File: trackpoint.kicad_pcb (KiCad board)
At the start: 2 copper layers, 27.5 x 24 mm, 9 parts

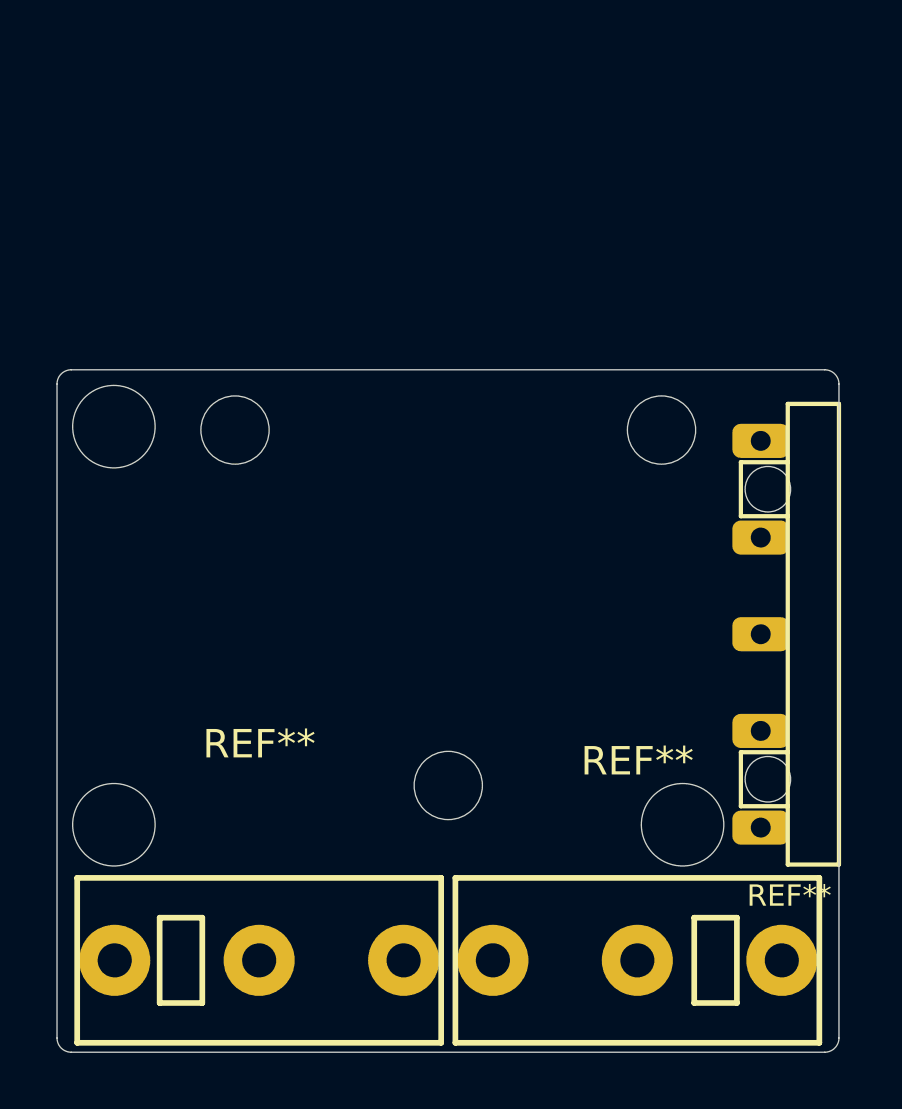
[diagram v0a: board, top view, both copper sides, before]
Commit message: Update board based on new CAD design.
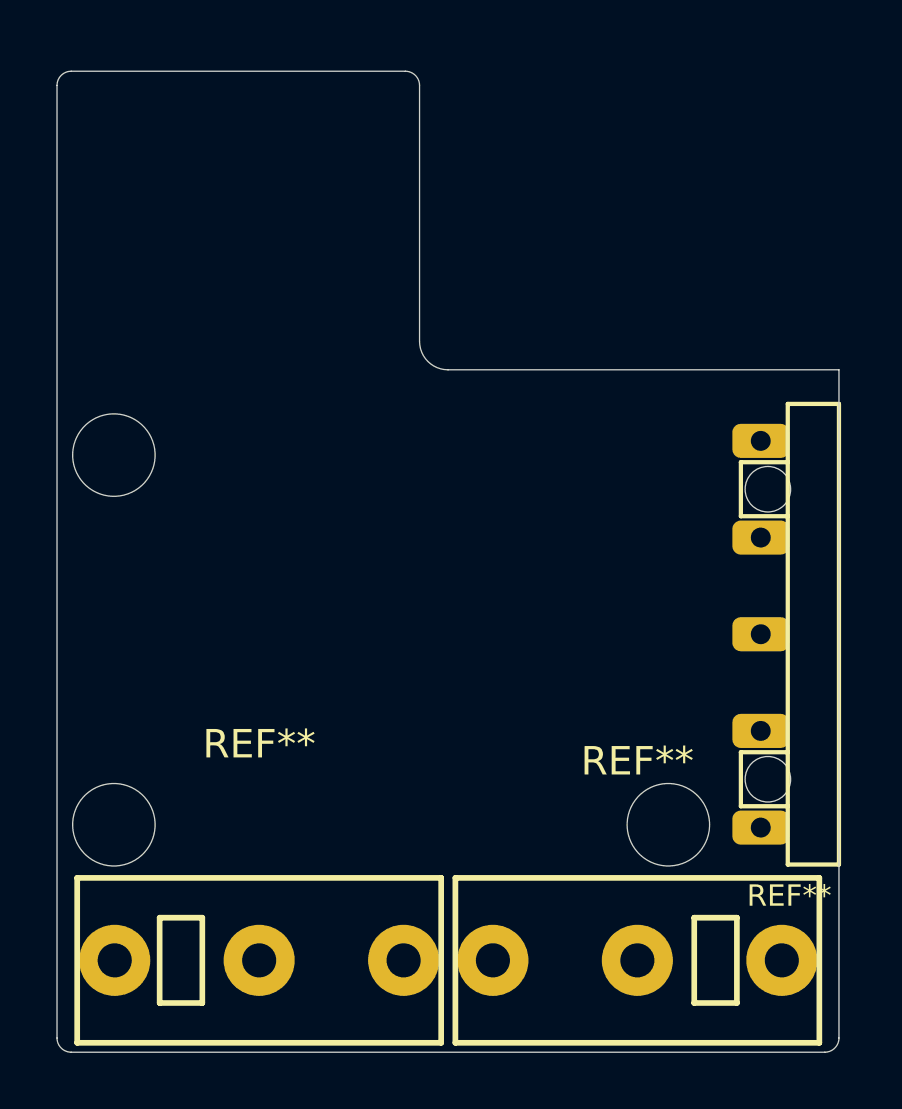
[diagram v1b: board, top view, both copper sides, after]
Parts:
- removed the ? at (194.2, 125.5)
- removed the ? at (206.0, 138.1)
- removed the ? at (213.5, 125.6)
- removed the ? at (198.5, 125.6)
- removed the ? at (214.2, 139.5)
- added ?: , UGL:hole_2.9000000953674316mm, F.Cu at (194.2, 126.5)
- added ?: , UGL:hole_2.9000000953674316mm, F.Cu at (213.8, 139.5)
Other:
- board size 27.5 x 24 mm -> 27.5 x 34.5 mm
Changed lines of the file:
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@@
   (general
     (thickness 1.6)
-    (drawings 9)
+    (drawings 20)
     (tracks 0)
     (zones 0)
-    (modules 9)
+    (modules 6)
     (nets 1)
   )
@@
   )
   (module UGL:hole_2.9000000953674316mm locked (layer F.Cu)
-    (at 194.25 125.5)
+    (at 194.25 126.5)
     (attr virtual)
     (fp_text reference "" (at 0 0) (layer F.SilkS)
@@
       (clearance 0.00001))
   )
-  (module UGL:hole_2.4000000953674316mm locked (layer F.Cu)
-    (at 206.010002 138.119003)
-    (attr virtual)
-    (fp_text reference "" (at 0 0) (layer F.SilkS)
-      (effects (font (size 1.27 1.27) (thickness 0.15)))
-    )
-    (fp_text value "" (at 0 0) (layer F.SilkS)
-      (effects (font (size 1.27 1.27) (thickness 0.15)))
-    )
-    (pad "" np_thru_hole circle (at 0 0) (size 2.4 2.4) (drill 2.4) (layers *.Cu *.Mask F.SilkS)
-      (clearance 0.00001))
-  )
-  (module UGL:hole_2.4000000953674316mm locked (layer F.Cu)
-    (at 213.510002 125.619003)
-    (attr virtual)
-    (fp_text reference "" (at 0 0) (layer F.SilkS)
-      (effects (font (size 1.27 1.27) (thickness 0.15)))
-    )
-    (fp_text value "" (at 0 0) (layer F.SilkS)
-      (effects (font (size 1.27 1.27) (thickness 0.15)))
-    )
-    (pad "" np_thru_hole circle (at 0 0) (size 2.4 2.4) (drill 2.4) (layers *.Cu *.Mask F.SilkS)
-      (clearance 0.00001))
-  )
-  (module UGL:hole_2.4000000953674316mm locked (layer F.Cu)
-    (at 198.510002 125.619003)
-    (attr virtual)
-    (fp_text reference "" (at 0 0) (layer F.SilkS)
-      (effects (font (size 1.27 1.27) (thickness 0.15)))
-    )
-    (fp_text value "" (at 0 0) (layer F.SilkS)
-      (effects (font (size 1.27 1.27) (thickness 0.15)))
-    )
-    (pad "" np_thru_hole circle (at 0 0) (size 2.4 2.4) (drill 2.4) (layers *.Cu *.Mask F.SilkS)
-      (clearance 0.00001))
-  )
   (module UGL:hole_2.9000000953674316mm locked (layer F.Cu)
-    (at 214.25 139.5)
+    (at 213.75 139.5)
     (attr virtual)
     (fp_text reference "" (at 0 0) (layer F.SilkS)
@@
       (clearance 0.00001))
   )
+  (gr_line (start 204.5 113) (end 192.75 113) (angle 90) (layer Edge.Cuts) (width 0.01))
+  (gr_line (start 192.25 113.5) (end 192.25 147) (angle 90) (layer Edge.Cuts) (width 0.01))
+  (gr_line (start 219.75 123.5) (end 206 123.5) (angle 90) (layer Edge.Cuts) (width 0.01))
   (gr_text "PCB ID: trackpoint_main_0.1.0" (at 206.1 146.5) (layer B.SilkS)
     (effects (font (size 1 1) (thickness 0.2)) (justify mirror))
   )
-  (gr_arc (start 192.75 124.000007) (end 192.75 123.5) (angle -90.00451968) (layer Edge.Cuts) (width 0.01))
   (gr_arc (start 192.75 146.999993) (end 192.25 147) (angle -89.99010657) (layer Edge.Cuts) (width 0.01))
   (gr_arc (start 219.25 146.999993) (end 219.25 147.5) (angle -90.00451968) (layer Edge.Cuts) (width 0.01))
-  (gr_arc (start 219.25 124.000007) (end 219.75 124) (angle -89.99010657) (layer Edge.Cuts) (width 0.01))
-  (gr_line (start 219.25 123.5) (end 192.75 123.5) (angle 90) (layer Edge.Cuts) (width 0.01))
-  (gr_line (start 192.25 124) (end 192.25 147) (angle 90) (layer Edge.Cuts) (width 0.01))
   (gr_line (start 192.75 147.5) (end 219.25 147.5) (angle 90) (layer Edge.Cuts) (width 0.01))
-  (gr_line (start 219.75 147) (end 219.75 124) (angle 90) (layer Edge.Cuts) (width 0.01))
+  (gr_circle (center 210.760002 135.119003) (end 210.760002 137.019003) (layer F.Adhes) (width 0.01))
+  (gr_circle (center 201.260002 135.119003) (end 201.260002 137.019003) (layer F.Adhes) (width 0.01))
+  (gr_circle (center 194.25 139.5) (end 195.9 139.5) (layer Eco1.User) (width 0.01))
+  (gr_circle (center 213.75 139.5) (end 215.4 139.5) (layer Eco1.User) (width 0.01))
+  (gr_circle (center 194.25 126.5) (end 195.9 126.5) (layer Eco1.User) (width 0.01))
+  (gr_circle (center 201.260002 125.619003) (end 201.260002 127.519003) (layer F.Adhes) (width 0.01))
+  (gr_circle (center 210.760002 125.619003) (end 210.760002 127.519003) (layer F.Adhes) (width 0.01))
+  (gr_circle (center 194.199997 118.468994) (end 194.199997 118.718994) (layer F.Adhes) (width 0.01))
+  (gr_arc (start 205.999992 122.500001) (end 205 122.5) (angle -90) (layer Edge.Cuts) (width 0.01))
+  (gr_line (start 205 122.5) (end 205 113.5) (angle 90) (layer Edge.Cuts) (width 0.01))
+  (gr_arc (start 204.5 113.500007) (end 205 113.5) (angle -90) (layer Edge.Cuts) (width 0.01))
+  (gr_arc (start 192.75 113.500007) (end 192.75 113) (angle -90) (layer Edge.Cuts) (width 0.01))
+  (gr_line (start 219.75 147) (end 219.75 123.5) (angle 90) (layer Edge.Cuts) (width 0.01))
 )

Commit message: Add FFC connector.
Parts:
- added REF**: 84981-8, ugl:84981-8, F.Cu at (194.2, 118.5)
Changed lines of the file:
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@@
   (general
     (thickness 1.6)
-    (drawings 20)
+    (drawings 19)
     (tracks 0)
     (zones 0)
-    (modules 6)
+    (modules 7)
     (nets 1)
   )
   (page A3)
   (title_block
-    (title "UHK Trackpoint Module - Main")
+    (title "UHK Trackpoint Module")
     (rev 0.1.0)
     (company "Ultimate Gadget Laboratories Kft.")
@@
     (uvia_drill 0.127)
   )
+  (module ugl:84981-8 (layer F.Cu)
+    (at 194.199997 118.468994 270)
+    (descr "FFC connector")
+    (fp_text reference REF** (at 0 -7.800003 90) (layer F.SilkS)
+      (effects (font (size 0.75 0.75) (thickness 0.15)))
+    )
+    (fp_text value 84981-8 (at 0 0.8 90) (layer F.SilkS)
+      (effects (font (size 0.75 0.75) (thickness 0.15)))
+    )
+    (fp_line (start 5.5 -5.6) (end 4 -5.6) (layer F.SilkS) (width 0.15))
+    (fp_line (start -5.5 -5.6) (end -4 -5.6) (layer F.SilkS) (width 0.15))
+    (fp_line (start -4.5 0) (end 4.5 0) (layer F.SilkS) (width 0.15))
+    (fp_line (start 5.5 -1.8) (end 5.5 -5.6) (layer F.SilkS) (width 0.15))
+    (fp_line (start -5.5 -1.8) (end -5.5 -5.6) (layer F.SilkS) (width 0.15))
+    (pad 5 smd rect (at 0.5 -5.95 270) (size 0.6 1.7) (layers F.Cu F.Paste F.Mask))
+    (pad 4 smd rect (at -0.5 -5.95 270) (size 0.6 1.7) (layers F.Cu F.Paste F.Mask))
+    (pad 6 smd rect (at 1.5 -5.95 270) (size 0.6 1.7) (layers F.Cu F.Paste F.Mask))
+    (pad 3 smd rect (at -1.5 -5.95 270) (size 0.6 1.7) (layers F.Cu F.Paste F.Mask))
+    (pad "" smd rect (at 5.3 -0.7 270) (size 1.2 1.8) (layers F.Cu F.Paste F.Mask))
+    (pad "" smd rect (at -5.3 -0.7 270) (size 1.2 1.8) (layers F.Cu F.Paste F.Mask))
+    (pad 1 smd rect (at -3.5 -5.95 270) (size 0.6 1.7) (layers F.Cu F.Paste F.Mask))
+    (pad 8 smd rect (at 3.5 -5.95 270) (size 0.6 1.7) (layers F.Cu F.Paste F.Mask))
+    (pad 7 smd rect (at 2.5 -5.95 270) (size 0.6 1.7) (layers F.Cu F.Paste F.Mask))
+    (pad 2 smd rect (at -2.5 -5.95 270) (size 0.6 1.7) (layers F.Cu F.Paste F.Mask))
+  )
   (module ugl:CMI126603D08 locked (layer F.Cu)
     (at 199.360001 144.268997)
@@
   (gr_line (start 219.75 123.5) (end 206 123.5) (angle 90) (layer Edge.Cuts) (width 0.01))
   (gr_text "PCB ID: trackpoint_main_0.1.0" (at 206.1 146.5) (layer B.SilkS)
-    (effects (font (size 1 1) (thickness 0.2)) (justify mirror))
+    (effects (font (size 0.75 0.75) (thickness 0.15)) (justify mirror))
   )
   (gr_arc (start 192.75 146.999993) (end 192.25 147) (angle -89.99010657) (layer Edge.Cuts) (width 0.01))
@@
   (gr_circle (center 201.260002 125.619003) (end 201.260002 127.519003) (layer F.Adhes) (width 0.01))
   (gr_circle (center 210.760002 125.619003) (end 210.760002 127.519003) (layer F.Adhes) (width 0.01))
-  (gr_circle (center 194.199997 118.468994) (end 194.199997 118.718994) (layer F.Adhes) (width 0.01))
   (gr_arc (start 205.999992 122.500001) (end 205 122.5) (angle -90) (layer Edge.Cuts) (width 0.01))
   (gr_line (start 205 122.5) (end 205 113.5) (angle 90) (layer Edge.Cuts) (width 0.01))

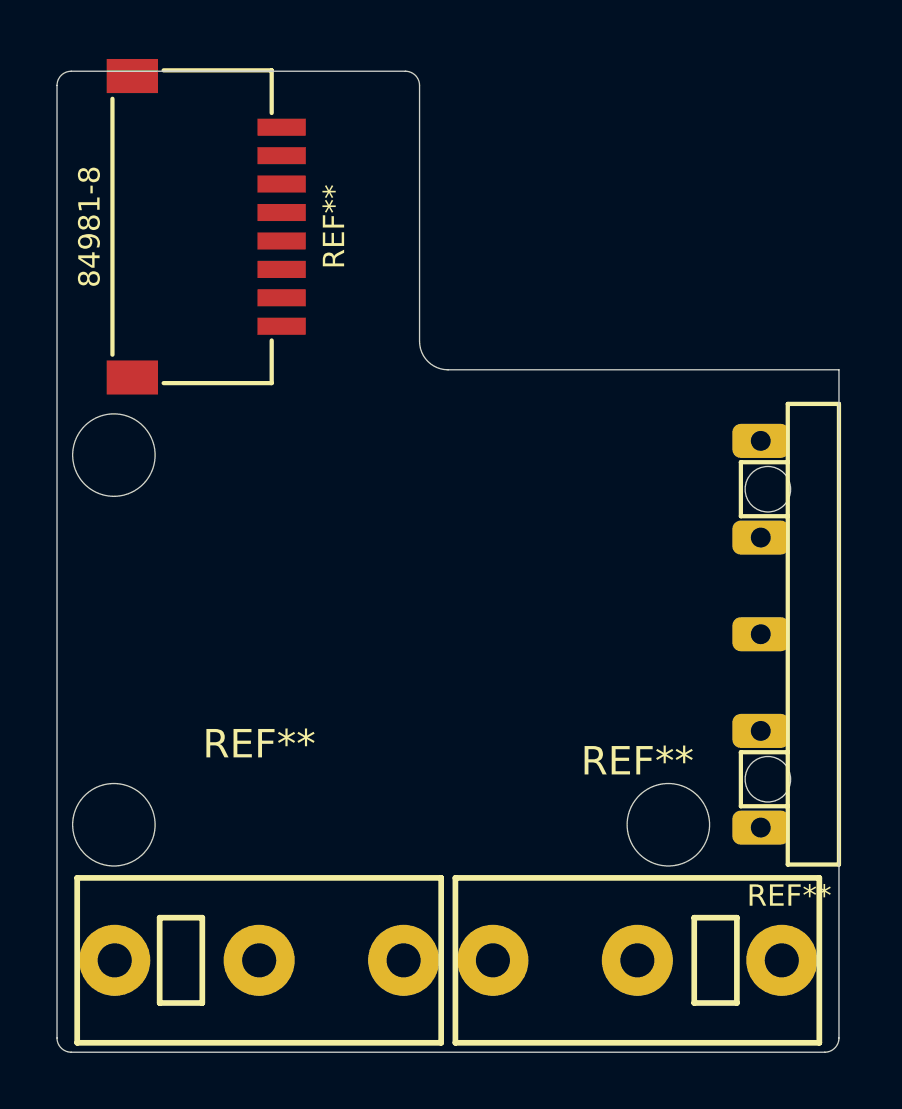
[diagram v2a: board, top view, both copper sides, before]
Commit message: Convert circles to holes.
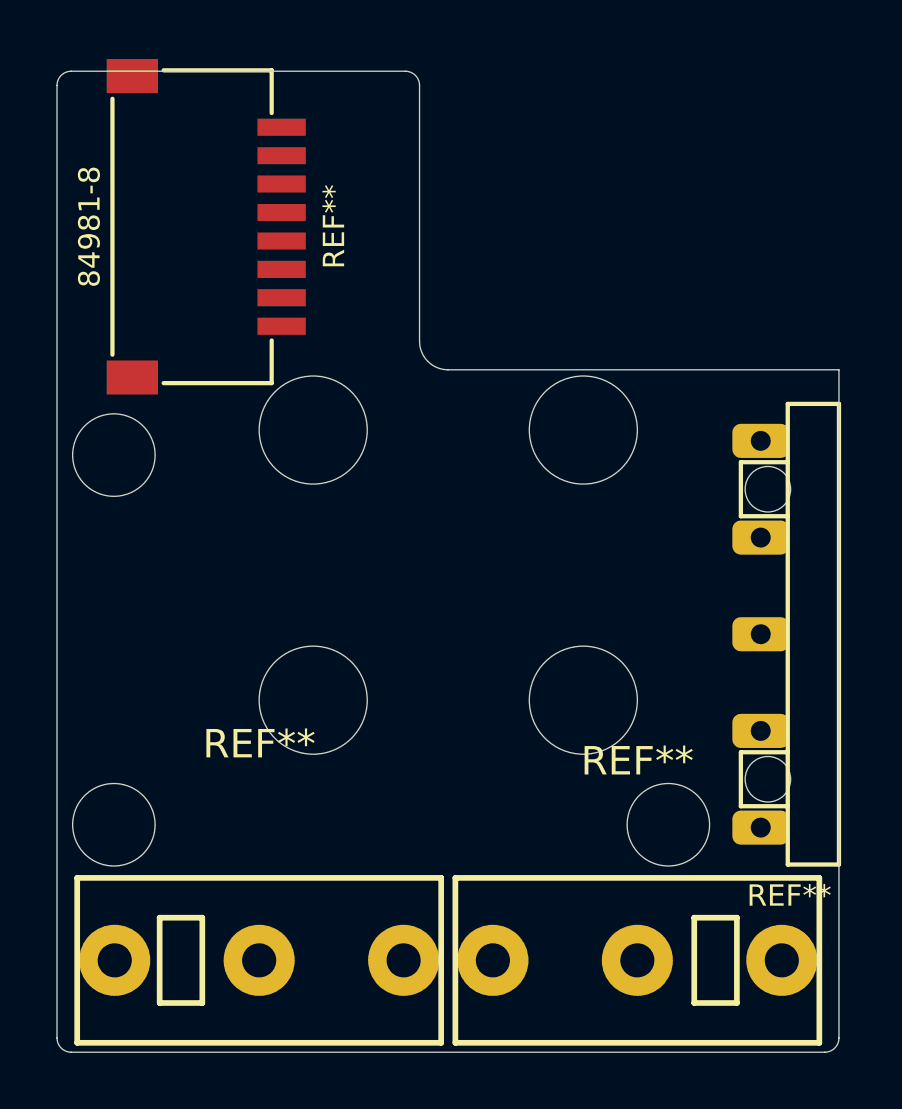
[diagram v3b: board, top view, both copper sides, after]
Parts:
- added ?: , UGL:hole_3.8000000000000114mm, F.Adhes at (210.8, 135.1)
- added ?: , UGL:hole_3.8000000000000114mm, F.Adhes at (201.3, 135.1)
- added ?: , UGL:hole_3.799999999999983mm, F.Adhes at (201.3, 125.6)
- added ?: , UGL:hole_3.799999999999983mm, F.Adhes at (210.8, 125.6)
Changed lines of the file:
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@@
   (gr_arc (start 219.25 146.999993) (end 219.25 147.5) (angle -90.00451968) (layer Edge.Cuts) (width 0.01))
   (gr_line (start 192.75 147.5) (end 219.25 147.5) (angle 90) (layer Edge.Cuts) (width 0.01))
-  (gr_circle (center 210.760002 135.119003) (end 210.760002 137.019003) (layer F.Adhes) (width 0.01))
-  (gr_circle (center 201.260002 135.119003) (end 201.260002 137.019003) (layer F.Adhes) (width 0.01))
+  (module UGL:hole_3.8000000000000114mm locked (layer F.Adhes)
+    (at 210.760002 135.119003)
+    (attr virtual)
+    (pad "" np_thru_hole circle (at 0 0) (size 3.8000000000000114 3.8000000000000114) (drill 3.8000000000000114) (layers *.Cu *.Mask F.SilkS)
+      (clearance 0.00001)
+    )
+  )
+  (module UGL:hole_3.8000000000000114mm locked (layer F.Adhes)
+    (at 201.260002 135.119003)
+    (attr virtual)
+    (pad "" np_thru_hole circle (at 0 0) (size 3.8000000000000114 3.8000000000000114) (drill 3.8000000000000114) (layers *.Cu *.Mask F.SilkS)
+      (clearance 0.00001)
+    )
+  )
   (gr_circle (center 194.25 139.5) (end 195.9 139.5) (layer Eco1.User) (width 0.01))
   (gr_circle (center 213.75 139.5) (end 215.4 139.5) (layer Eco1.User) (width 0.01))
   (gr_circle (center 194.25 126.5) (end 195.9 126.5) (layer Eco1.User) (width 0.01))
-  (gr_circle (center 201.260002 125.619003) (end 201.260002 127.519003) (layer F.Adhes) (width 0.01))
-  (gr_circle (center 210.760002 125.619003) (end 210.760002 127.519003) (layer F.Adhes) (width 0.01))
+  (module UGL:hole_3.799999999999983mm locked (layer F.Adhes)
+    (at 201.260002 125.619003)
+    (attr virtual)
+    (pad "" np_thru_hole circle (at 0 0) (size 3.799999999999983 3.799999999999983) (drill 3.799999999999983) (layers *.Cu *.Mask F.SilkS)
+      (clearance 0.00001)
+    )
+  )
+  (module UGL:hole_3.799999999999983mm locked (layer F.Adhes)
+    (at 210.760002 125.619003)
+    (attr virtual)
+    (pad "" np_thru_hole circle (at 0 0) (size 3.799999999999983 3.799999999999983) (drill 3.799999999999983) (layers *.Cu *.Mask F.SilkS)
+      (clearance 0.00001)
+    )
+  )
   (gr_arc (start 205.999992 122.500001) (end 205 122.5) (angle -90) (layer Edge.Cuts) (width 0.01))
   (gr_line (start 205 122.5) (end 205 113.5) (angle 90) (layer Edge.Cuts) (width 0.01))
